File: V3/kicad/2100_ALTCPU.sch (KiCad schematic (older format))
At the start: 26 parts, among them U2100 Z8-L180-S180-180-PQFP-80, U2101 GAL16V8, U2102 14.7456 MHz

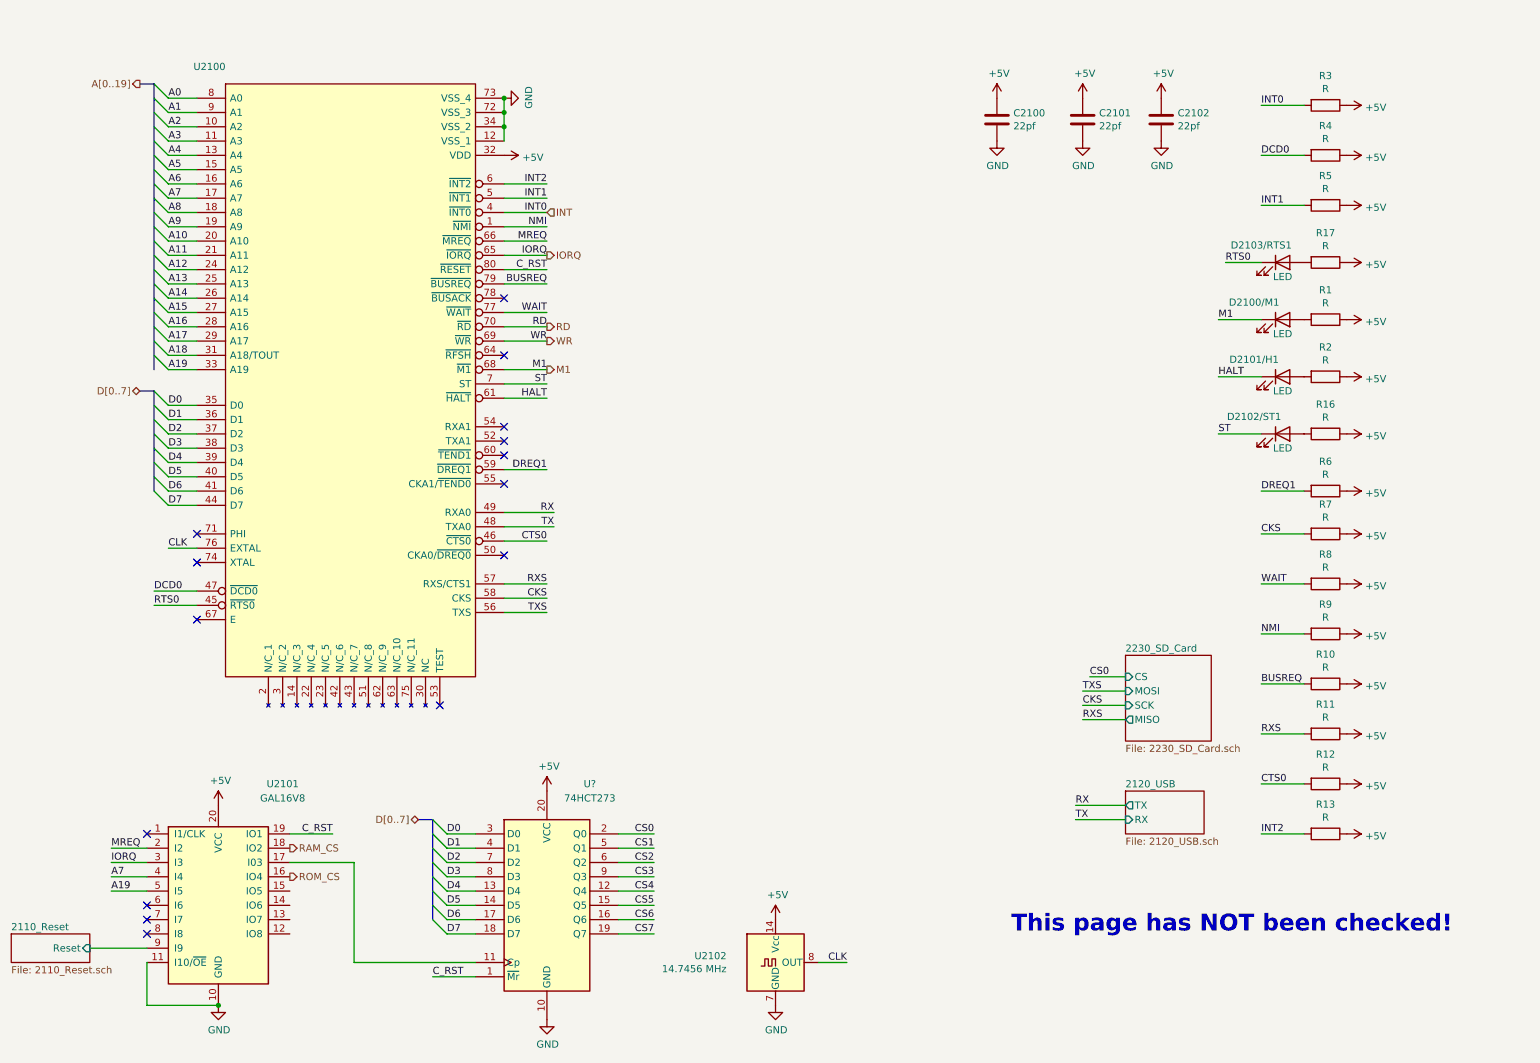
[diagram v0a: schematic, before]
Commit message: First two R arrays
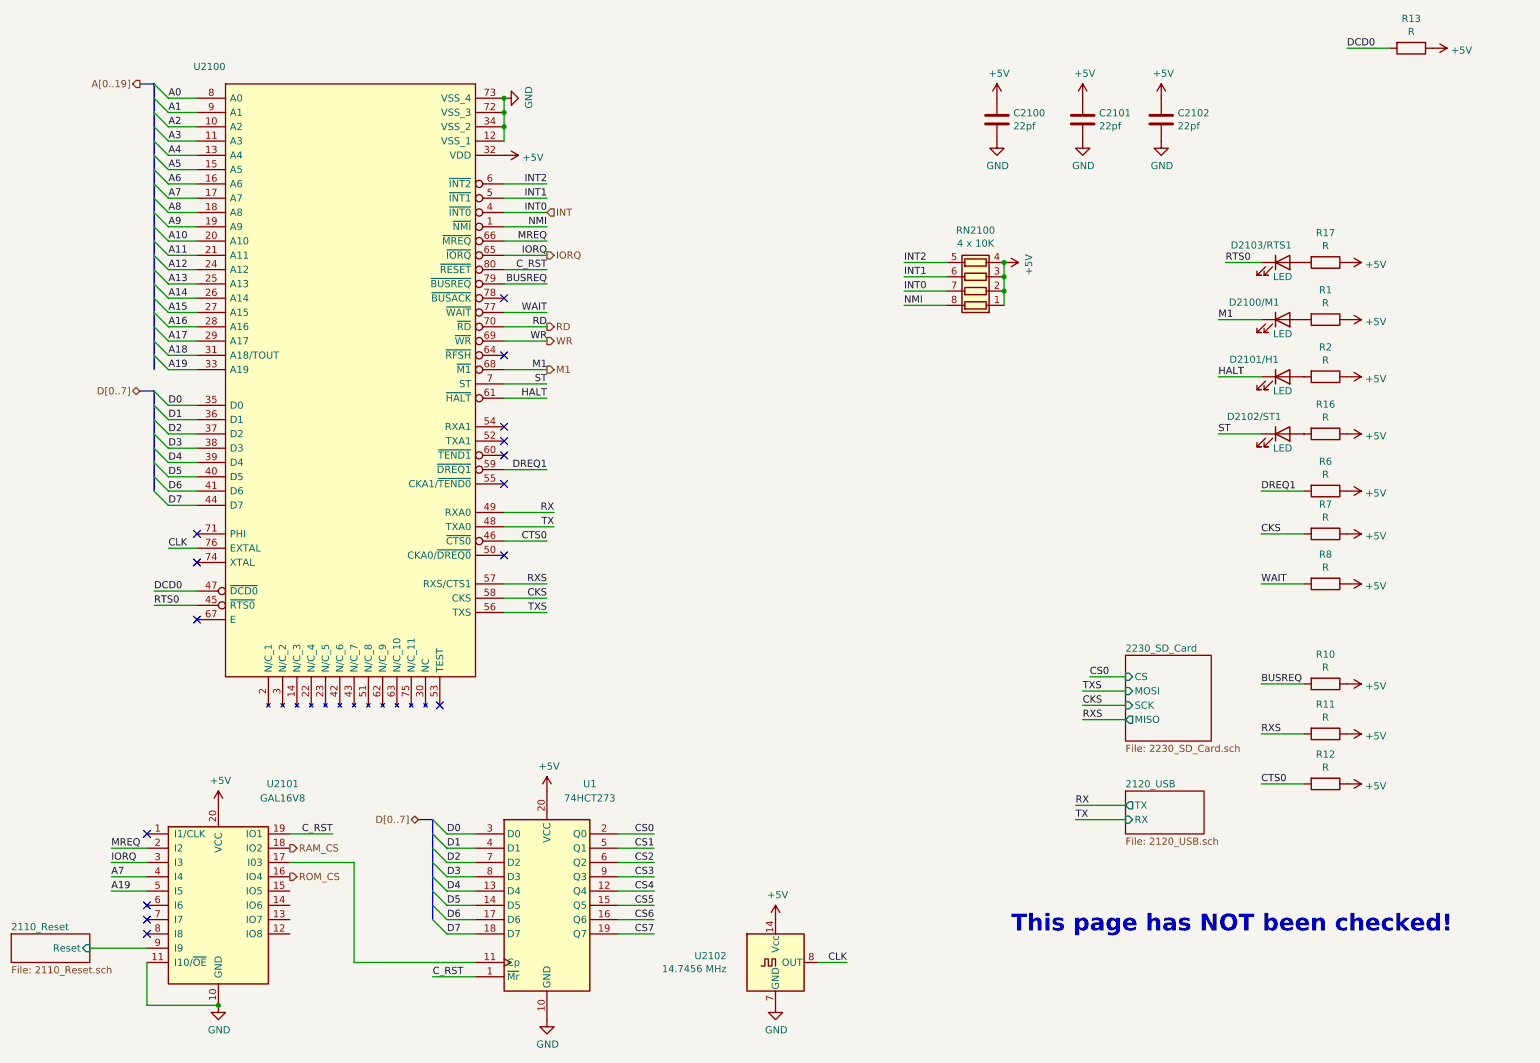
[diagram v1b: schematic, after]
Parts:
- removed R3, R4, R5, R9: R, Resistor_SMD:R_1206_3216Metric, symbol Device:R
- added RN2100: 4 x 10K, Resistor_SMD:R_Array_Convex_4x1206, symbol Device:R_Pack04
- gave numbers to parts that had none: 1
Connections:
- net +5V: now also RN2100.1 (R1.1), RN2100.2 (R2.1), RN2100.3 (R3.1), RN2100.4 (R4.1)
- net DCD0: now also R13.2
- net INT: now also RN2100.7 (R2.2)
- net INT1: now also RN2100.6 (R3.2)
- net INT2: now also RN2100.5 (R4.2); no longer R13.2
- net NMI: now also RN2100.8 (R1.2)
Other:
- moved on the sheet: R13
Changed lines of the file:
@@
 INT1
 Wire Wire Line
-	9750 6250 9450 6250
-Wire Wire Line
-	9750 1850 9450 1850
-Text Label 9450 6250 0    50   ~ 0
+	7250 2250 6950 2250
+Wire Wire Line
+	7250 2350 6950 2350
+Text Label 6950 2250 0    50   ~ 0
 INT2
-Text Label 9450 1850 0    50   ~ 0
+Text Label 6950 2350 0    50   ~ 0
 INT1
 Wire Wire Line
 	4150 2000 4450 2000
 Text Label 4450 2000 2    50   ~ 0
-NMI
-Wire Wire Line
-	9750 4850 9450 4850
-Text Label 9450 4850 0    50   ~ 0
 NMI
 Wire Wire Line
@@
 M1
 Wire Wire Line
-	9750 1150 9450 1150
-Text Label 9450 1150 0    50   ~ 0
+	7250 2450 6950 2450
+Text Label 6950 2450 0    50   ~ 0
 INT0
 Wire Wire Line
@@
 DCD0
 Wire Wire Line
-	9750 1500 9450 1500
-Text Label 9450 1500 0    50   ~ 0
+	10350 750  10050 750
+Text Label 10050 750  0    50   ~ 0
 DCD0
 NoConn ~ 3700 5350
@@
 $EndComp
 $Comp
-L Device:R R9
-U 1 1 62EFCD2B
-P 9900 4850
-F 0 "R9" V 9693 4850 50  0000 C CNN
-F 1 "R" V 9784 4850 50  0000 C CNN
-F 2 "Resistor_SMD:R_1206_3216Metric" V 9830 4850 50  0001 C CNN
-F 3 "~" H 9900 4850 50  0001 C CNN
-	1    9900 4850
-	0    1    1    0
-$EndComp
-$Comp
-L power:+5V #PWR0137
-U 1 1 62EFCD31
-P 10050 4850
-F 0 "#PWR0137" H 10050 4700 50  0001 C CNN
-F 1 "+5V" V 10065 4978 50  0000 L CNN
-F 2 "" H 10050 4850 50  0001 C CNN
-F 3 "" H 10050 4850 50  0001 C CNN
-	1    10050 4850
-	0    1    1    0
-$EndComp
-$Comp
 L Device:R R10
 U 1 1 62F00BDB
@@
 L Device:R R13
 U 1 1 62F0AE91
-P 9900 6250
-F 0 "R13" V 9693 6250 50  0000 C CNN
-F 1 "R" V 9784 6250 50  0000 C CNN
-F 2 "Resistor_SMD:R_1206_3216Metric" V 9830 6250 50  0001 C CNN
-F 3 "~" H 9900 6250 50  0001 C CNN
-	1    9900 6250
+P 10500 750
+F 0 "R13" V 10293 750 50  0000 C CNN
+F 1 "R" V 10384 750 50  0000 C CNN
+F 2 "Resistor_SMD:R_1206_3216Metric" V 10430 750 50  0001 C CNN
+F 3 "~" H 10500 750 50  0001 C CNN
+	1    10500 750
 	0    1    1    0
 $EndComp
@@
 L power:+5V #PWR0141
 U 1 1 62F0AE97
-P 10050 6250
-F 0 "#PWR0141" H 10050 6100 50  0001 C CNN
-F 1 "+5V" V 10065 6378 50  0000 L CNN
-F 2 "" H 10050 6250 50  0001 C CNN
-F 3 "" H 10050 6250 50  0001 C CNN
-	1    10050 6250
-	0    1    1    0
-$EndComp
-$Comp
-L Device:R R5
-U 1 1 62F3049F
-P 9900 1850
-F 0 "R5" V 9693 1850 50  0000 C CNN
-F 1 "R" V 9784 1850 50  0000 C CNN
-F 2 "Resistor_SMD:R_1206_3216Metric" V 9830 1850 50  0001 C CNN
-F 3 "~" H 9900 1850 50  0001 C CNN
-	1    9900 1850
-	0    1    1    0
-$EndComp
-$Comp
-L power:+5V #PWR0142
-U 1 1 62F304A5
-P 10050 1850
-F 0 "#PWR0142" H 10050 1700 50  0001 C CNN
-F 1 "+5V" V 10065 1978 50  0000 L CNN
-F 2 "" H 10050 1850 50  0001 C CNN
-F 3 "" H 10050 1850 50  0001 C CNN
-	1    10050 1850
-	0    1    1    0
-$EndComp
-$Comp
-L Device:R R4
-U 1 1 62F33CBD
-P 9900 1500
-F 0 "R4" V 9693 1500 50  0000 C CNN
-F 1 "R" V 9784 1500 50  0000 C CNN
-F 2 "Resistor_SMD:R_1206_3216Metric" V 9830 1500 50  0001 C CNN
-F 3 "~" H 9900 1500 50  0001 C CNN
-	1    9900 1500
-	0    1    1    0
-$EndComp
-$Comp
-L power:+5V #PWR0143
-U 1 1 62F33CC3
-P 10050 1500
-F 0 "#PWR0143" H 10050 1350 50  0001 C CNN
-F 1 "+5V" V 10065 1628 50  0000 L CNN
-F 2 "" H 10050 1500 50  0001 C CNN
-F 3 "" H 10050 1500 50  0001 C CNN
-	1    10050 1500
-	0    1    1    0
-$EndComp
-$Comp
-L Device:R R3
-U 1 1 62F3762F
-P 9900 1150
-F 0 "R3" V 9693 1150 50  0000 C CNN
-F 1 "R" V 9784 1150 50  0000 C CNN
-F 2 "Resistor_SMD:R_1206_3216Metric" V 9830 1150 50  0001 C CNN
-F 3 "~" H 9900 1150 50  0001 C CNN
-	1    9900 1150
-	0    1    1    0
-$EndComp
-$Comp
-L power:+5V #PWR0153
-U 1 1 62F37635
-P 10050 1150
-F 0 "#PWR0153" H 10050 1000 50  0001 C CNN
-F 1 "+5V" V 10065 1278 50  0000 L CNN
-F 2 "" H 10050 1150 50  0001 C CNN
-F 3 "" H 10050 1150 50  0001 C CNN
-	1    10050 1150
+P 10650 750
+F 0 "#PWR0141" H 10650 600 50  0001 C CNN
+F 1 "+5V" V 10665 878 50  0000 L CNN
+F 2 "" H 10650 750 50  0001 C CNN
+F 3 "" H 10650 750 50  0001 C CNN
+	1    10650 750
 	0    1    1    0
 $EndComp
@@
 TXS
 $Comp
-L 74xx:74HCT273 U?
+L 74xx:74HCT273 U1
 U 1 1 63802B80
 P 4450 6750
-F 0 "U?" H 4750 7600 50  0000 C CNN
+F 0 "U1" H 4750 7600 50  0000 C CNN
 F 1 "74HCT273" H 4750 7500 50  0000 C CNN
 F 2 "" H 4450 6750 50  0001 C CNN
@@
 AR Path="/6191B6A2/61F0BDAE/638069B9" Ref="#PWR?"  Part="1"
 AR Path="/6195D2C9/638069B9" Ref="#PWR?"  Part="1"
-AR Path="/6191B6A2/61EBDADB/638069B9" Ref="#PWR?"  Part="1"
-F 0 "#PWR?" H 4450 7300 50  0001 C CNN
+AR Path="/6191B6A2/61EBDADB/638069B9" Ref="#PWR0150"  Part="1"
+F 0 "#PWR0150" H 4450 7300 50  0001 C CNN
 F 1 "GND" H 4455 7377 50  0000 C CNN
 F 2 "" H 4450 7550 50  0001 C CNN
@@
 P 4450 5950
 AR Path="/6191B6A2/6380B8FC" Ref="#PWR?"  Part="1"
-AR Path="/6191B6A2/61EBDADB/6380B8FC" Ref="#PWR?"  Part="1"
-F 0 "#PWR?" H 4450 5800 50  0001 C CNN
+AR Path="/6191B6A2/61EBDADB/6380B8FC" Ref="#PWR0157"  Part="1"
+F 0 "#PWR0157" H 4450 5800 50  0001 C CNN
 F 1 "+5V" H 4465 6123 50  0000 C CNN
 F 2 "" H 4450 5950 50  0001 C CNN
@@
 	2000 4250 1800 4250
 NoConn ~ 2000 4150
+$Comp
+L Device:R_Pack04 RN?
+U 1 1 63966909
+P 7450 2350
+AR Path="/6191B6A2/61EBDADB/636B5B34/63966909" Ref="RN?"  Part="1"
+AR Path="/6191B6A2/61EBDADB/63966909" Ref="RN2100"  Part="1"
+F 0 "RN2100" V 7775 2350 50  0000 C CNN
+F 1 "4 x 10K" V 7684 2350 50  0000 C CNN
+F 2 "Resistor_SMD:R_Array_Convex_4x1206" V 7725 2350 50  0001 C CNN
+F 3 "~" H 7450 2350 50  0001 C CNN
+	1    7450 2350
+	0    -1   -1   0
+$EndComp
+$Comp
+L power:+5V #PWR?
+U 1 1 63978B22
+P 7650 2250
+AR Path="/6195D2C9/63978B22" Ref="#PWR?"  Part="1"
+AR Path="/6191B6A2/61F28B7D/63978B22" Ref="#PWR?"  Part="1"
+AR Path="/6191B6A2/61EBDADB/63978B22" Ref="#PWR0142"  Part="1"
+F 0 "#PWR0142" H 7650 2100 50  0001 C CNN
+F 1 "+5V" H 7665 2423 50  0000 C CNN
+F 2 "" H 7650 2250 50  0001 C CNN
+F 3 "" H 7650 2250 50  0001 C CNN
+	1    7650 2250
+	0    1    1    0
+$EndComp
+Wire Wire Line
+	7650 2550 7650 2450
+Connection ~ 7650 2250
+Connection ~ 7650 2350
+Wire Wire Line
+	7650 2350 7650 2250
+Connection ~ 7650 2450
+Wire Wire Line
+	7650 2450 7650 2350
+Wire Wire Line
+	7250 2550 6950 2550
+Text Label 6950 2550 0    50   ~ 0
+NMI
 Wire Bus Line
 	1700 3150 1700 3850
